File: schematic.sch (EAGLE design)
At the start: 56 parts, among them J1 FTDI_DEVICERA_SMT, M1 WIRELESS-NRF24L01, Q1 8MHz, T1 NMOS, T2 NMOS, T3 NMOS, T4 NMOS, U1 ATMEGA328P_TQFP, U2 GY-521MPU6050, U3 LTC3534

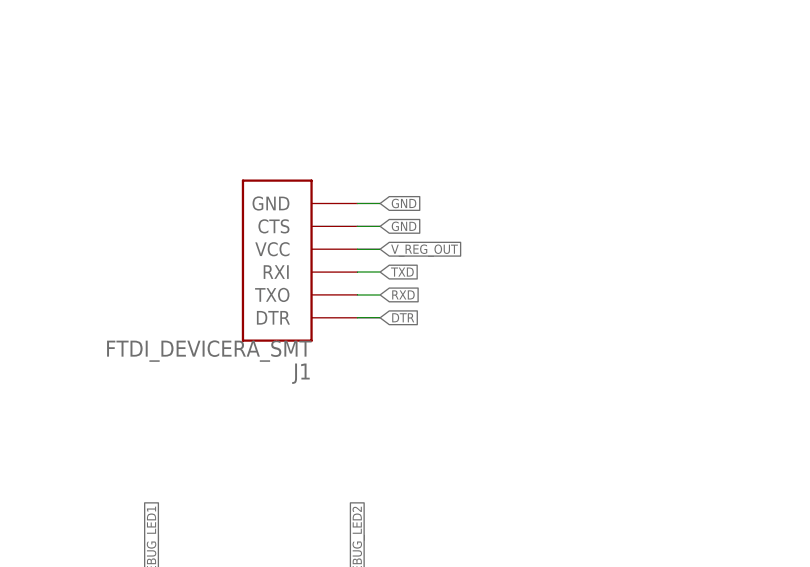
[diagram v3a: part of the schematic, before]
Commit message: fixed programmer RX TX
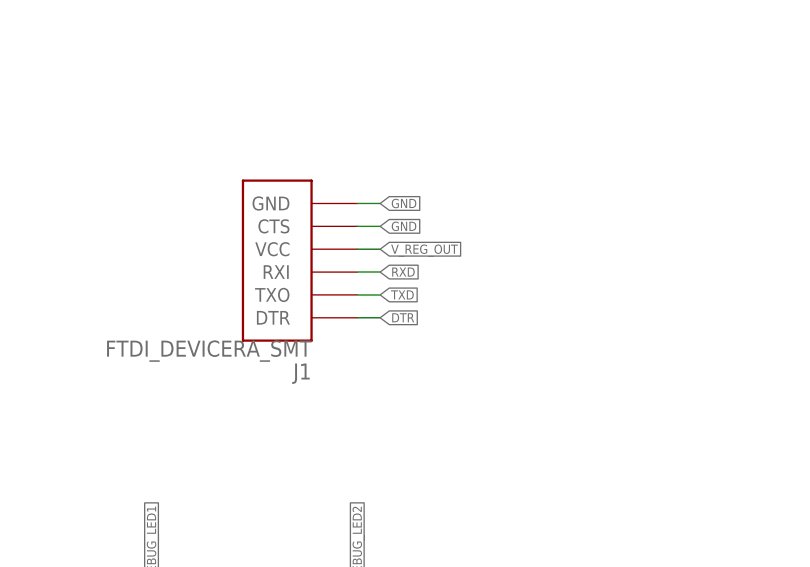
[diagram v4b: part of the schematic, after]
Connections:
- net RXD: now also J1.RXI; no longer J1.TXO
- net TXD: now also J1.TXO; no longer J1.RXI
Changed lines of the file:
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@@
 <net name="TXD" class="0">
-<segment>
-<pinref part="J1" gate="G$1" pin="RXI"/>
-<wire x1="-38.1" y1="15.24" x2="-35.56" y2="15.24" width="0.1524" layer="91"/>
-<label x="-35.56" y="15.24" size="1.016" layer="95" ratio="4" xref="yes"/>
-</segment>
 <segment>
 <pinref part="U1" gate="U$1" pin="PD1(TXD)"/>
@@
 <label x="228.6" y="81.28" size="1.016" layer="95" ratio="4" xref="yes"/>
 </segment>
-</net>
-<net name="RXD" class="0">
 <segment>
 <pinref part="J1" gate="G$1" pin="TXO"/>
 <wire x1="-38.1" y1="12.7" x2="-35.56" y2="12.7" width="0.1524" layer="91"/>
-<label x="-35.56" y="12.7" size="1.016" layer="95" ratio="4" xref="yes"/>
+<label x="-35.56" y="12.7" size="1.016" layer="95" xref="yes"/>
 </segment>
+</net>
+<net name="RXD" class="0">
 <segment>
 <pinref part="U1" gate="U$1" pin="PD0(RXD)"/>
@@
 <label x="228.6" y="83.82" size="1.016" layer="95" ratio="4" xref="yes"/>
 </segment>
+<segment>
+<pinref part="J1" gate="G$1" pin="RXI"/>
+<wire x1="-38.1" y1="15.24" x2="-35.56" y2="15.24" width="0.1524" layer="91"/>
+<label x="-35.56" y="15.24" size="1.016" layer="95" xref="yes"/>
+</segment>
 </net>

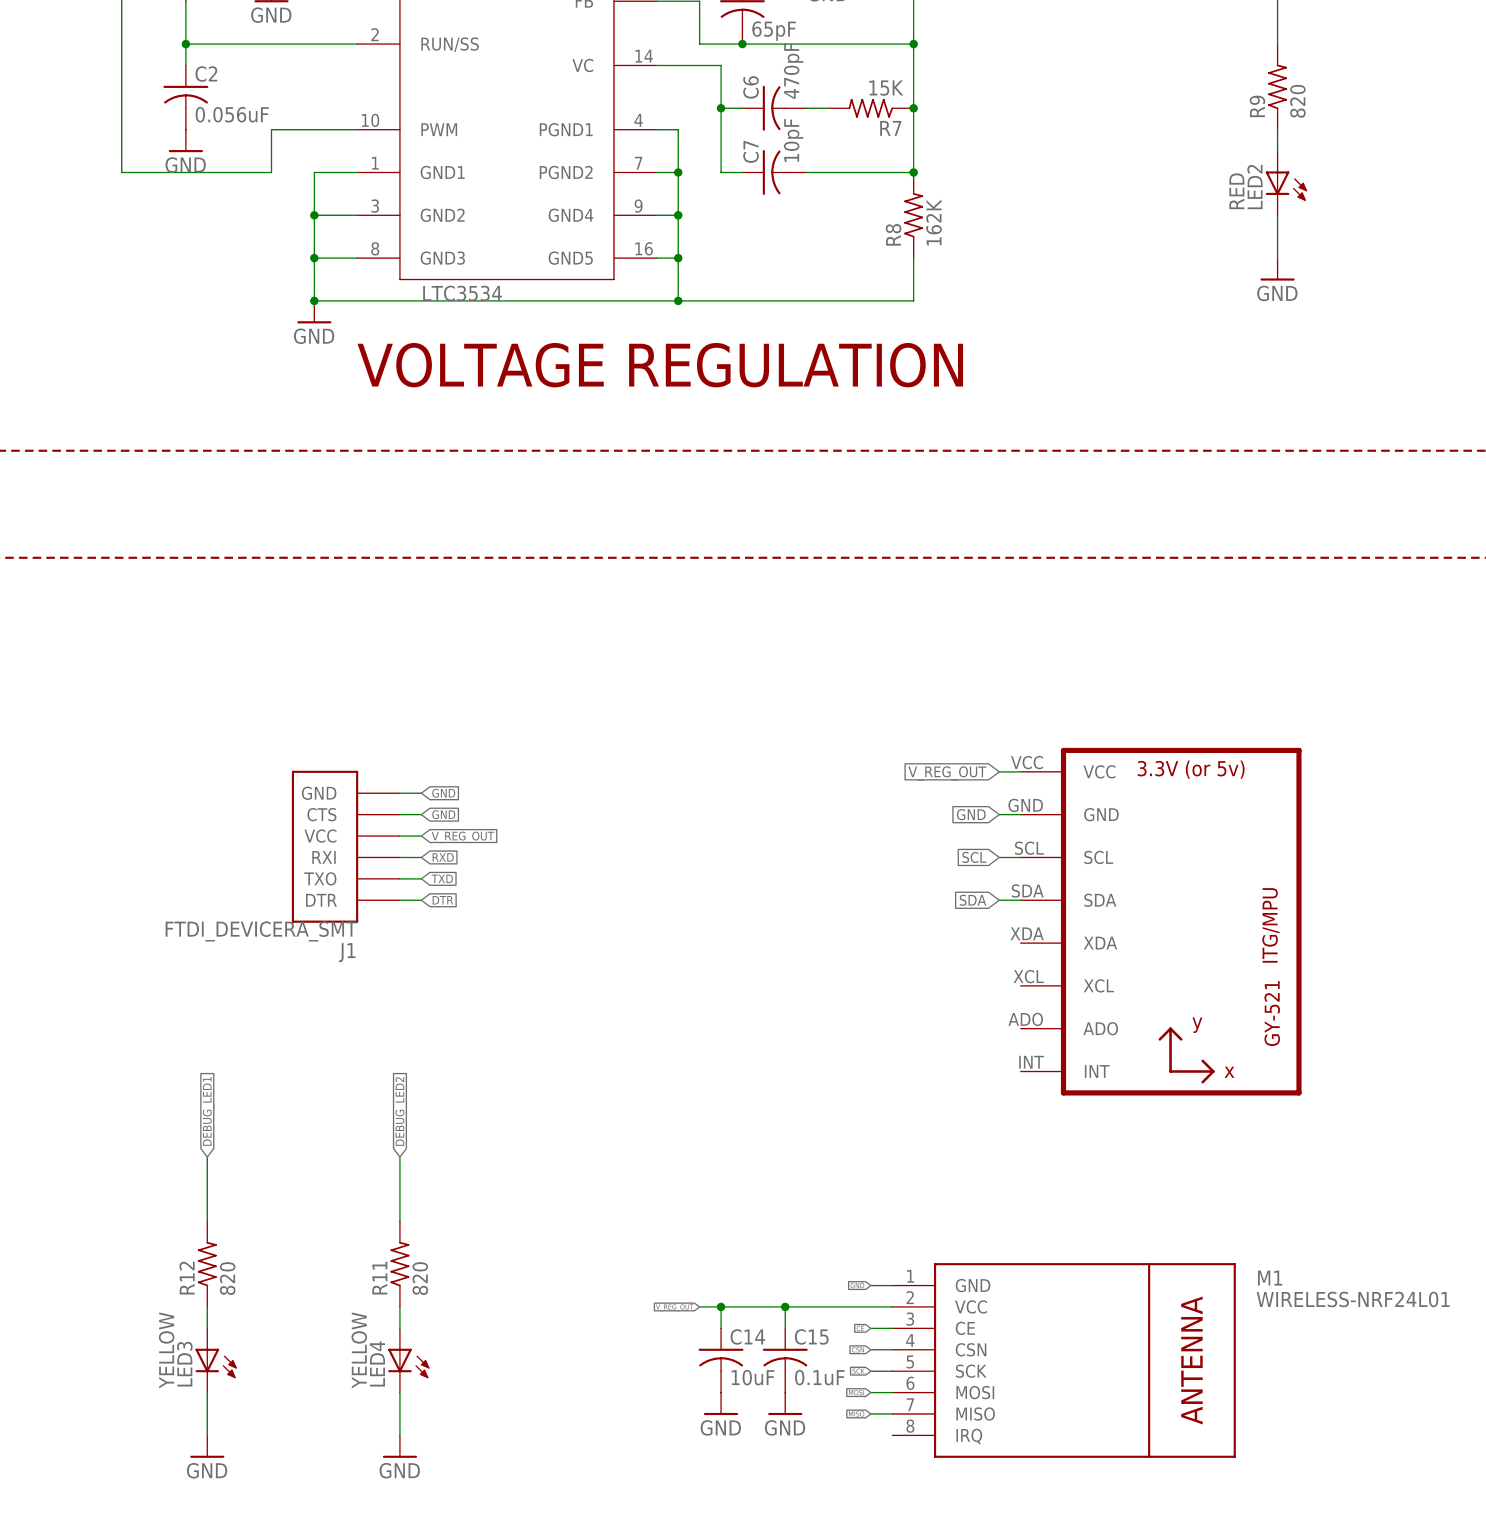
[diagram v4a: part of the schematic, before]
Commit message: Fixed LED package
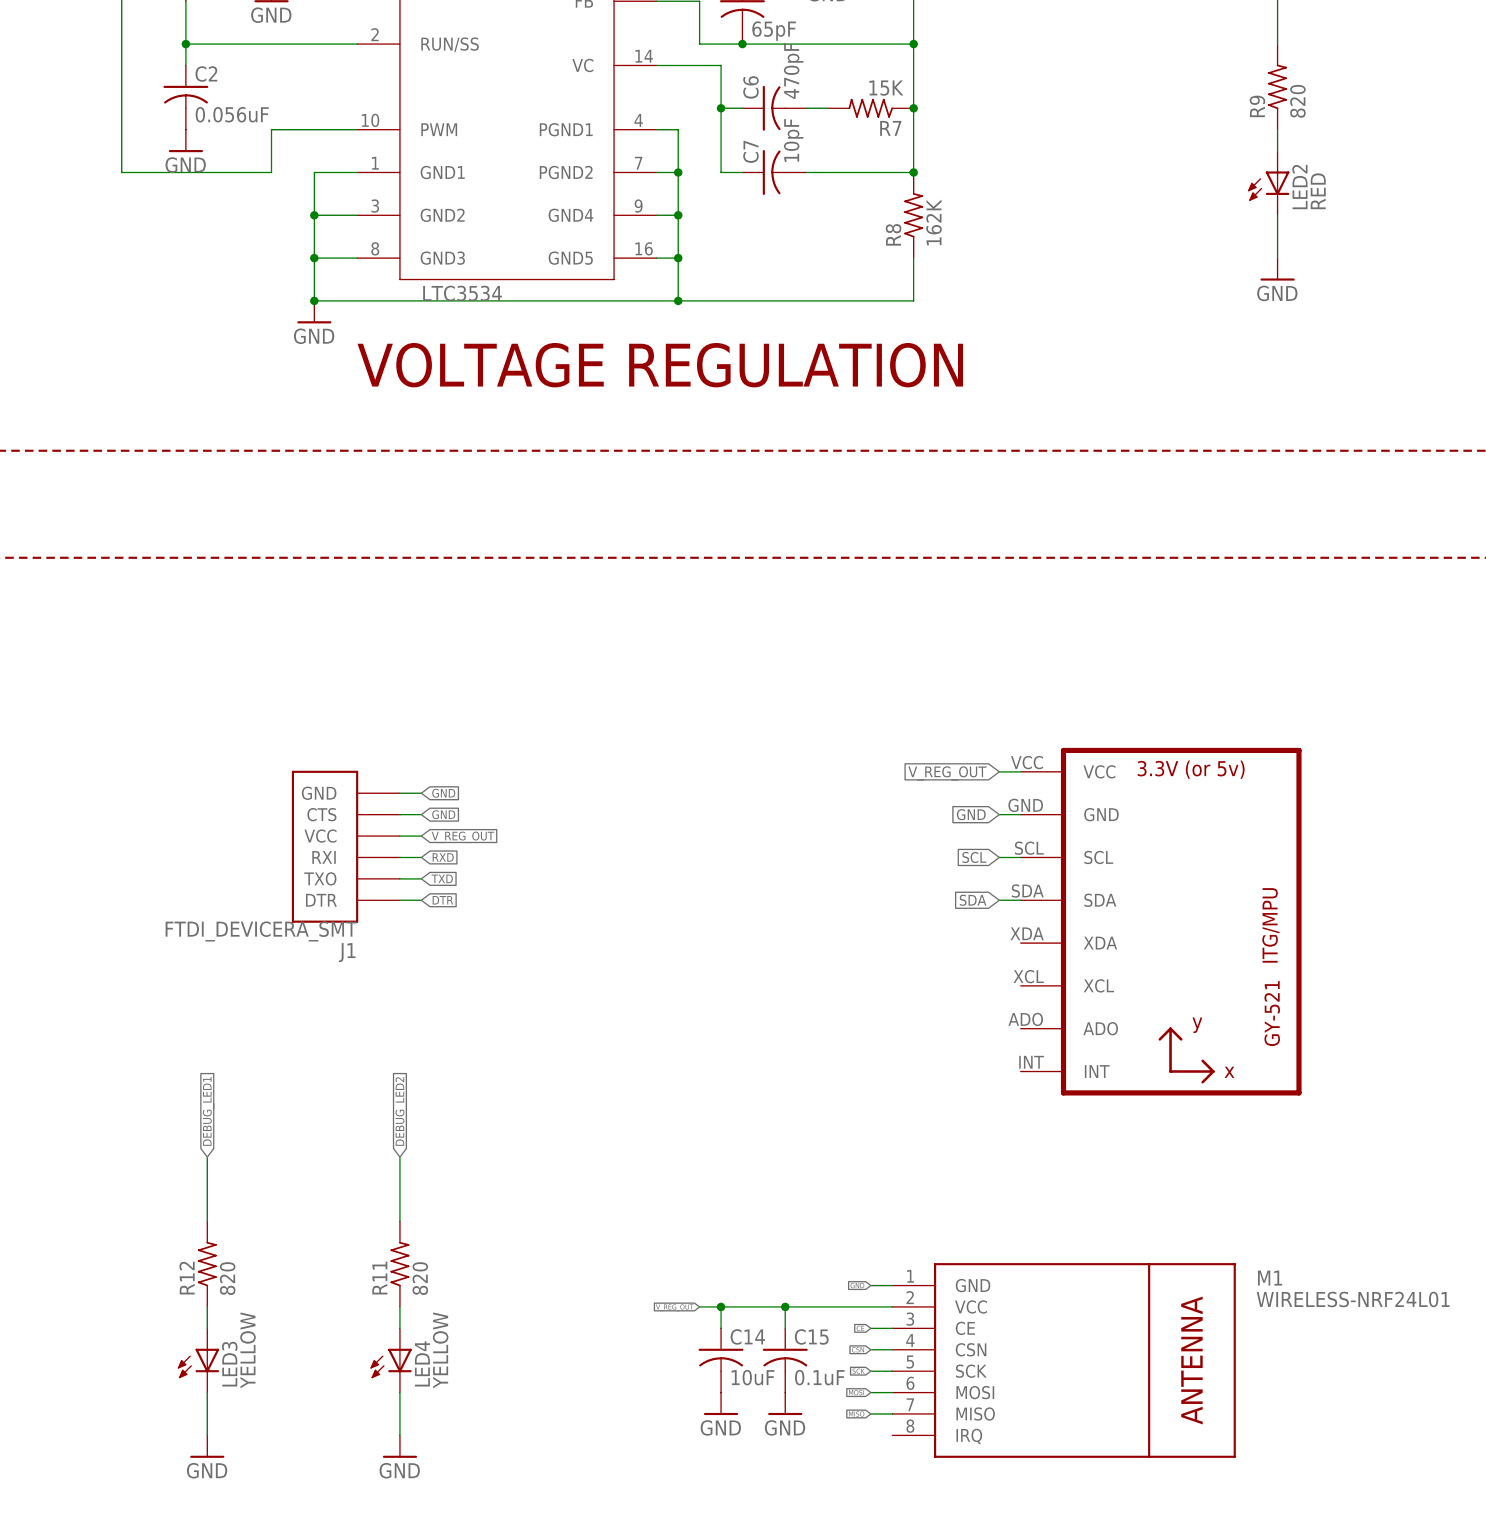
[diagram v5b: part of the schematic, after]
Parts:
- LED3, LED4: device led:LED -> led:LEDSML0603
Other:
- moved on the sheet: LED2, LED3, LED4
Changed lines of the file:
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@@
 <part name="GND28" library="SparkFun" deviceset="GND" device=""/>
 <part name="GND29" library="SparkFun" deviceset="GND" device=""/>
-<part name="LED3" library="led" library_urn="urn:adsk.eagle:library:259" deviceset="LED" device="" package3d_urn="urn:adsk.eagle:package:15825/1" value="YELLOW"/>
 <part name="GND30" library="SparkFun" deviceset="GND" device=""/>
-<part name="LED4" library="led" library_urn="urn:adsk.eagle:library:259" deviceset="LED" device="" package3d_urn="urn:adsk.eagle:package:15825/1" value="YELLOW"/>
 <part name="GND31" library="SparkFun" deviceset="GND" device=""/>
 <part name="GND32" library="SparkFun" deviceset="GND" device=""/>
@@
 <part name="R12" library="rcl" library_urn="urn:adsk.eagle:library:334" deviceset="R-US_" device="R0603" package3d_urn="urn:adsk.eagle:package:23555/2" value="820"/>
 <part name="R11" library="rcl" library_urn="urn:adsk.eagle:library:334" deviceset="R-US_" device="R0603" package3d_urn="urn:adsk.eagle:package:23555/2" value="820"/>
-<part name="LED1" library="led" library_urn="urn:adsk.eagle:library:259" deviceset="LED" device="SML0603" package3d_urn="urn:adsk.eagle:package:15832/1" value="RED"/>
-<part name="LED2" library="led" library_urn="urn:adsk.eagle:library:259" deviceset="LED" device="SML0603" package3d_urn="urn:adsk.eagle:package:15832/1" value="RED"/>
 <part name="R10" library="resistor" library_urn="urn:adsk.eagle:library:348" deviceset="R-US_" device="R0603" package3d_urn="urn:adsk.eagle:package:26057/1" value="10K"/>
 <part name="R13" library="resistor" library_urn="urn:adsk.eagle:library:348" deviceset="R-US_" device="R0603" package3d_urn="urn:adsk.eagle:package:26057/1" value="10K"/>
@@
 <part name="R16" library="resistor" library_urn="urn:adsk.eagle:library:348" deviceset="R-US_" device="R0603" package3d_urn="urn:adsk.eagle:package:26057/1" value="10K"/>
 <part name="C4" library="rcl" library_urn="urn:adsk.eagle:library:334" deviceset="C-US" device="C1206" package3d_urn="urn:adsk.eagle:package:23618/2" value="65pF"/>
+<part name="LED1" library="led" library_urn="urn:adsk.eagle:library:259" deviceset="LED" device="SML0603" package3d_urn="urn:adsk.eagle:package:15832/1" value="RED"/>
+<part name="LED2" library="led" library_urn="urn:adsk.eagle:library:259" deviceset="LED" device="SML0603" package3d_urn="urn:adsk.eagle:package:15832/1" value="RED"/>
+<part name="LED3" library="led" library_urn="urn:adsk.eagle:library:259" deviceset="LED" device="SML0603" package3d_urn="urn:adsk.eagle:package:15832/1" value="YELLOW"/>
+<part name="LED4" library="led" library_urn="urn:adsk.eagle:library:259" deviceset="LED" device="SML0603" package3d_urn="urn:adsk.eagle:package:15832/1" value="YELLOW"/>
 </parts>
 <sheets>
@@
 <instance part="GND28" gate="1" x="-193.04" y="-73.66"/>
 <instance part="GND29" gate="1" x="-144.78" y="-73.66"/>
-<instance part="LED3" gate="G$1" x="-60.96" y="-43.18" rot="MR0"/>
 <instance part="GND30" gate="1" x="-60.96" y="-55.88"/>
-<instance part="LED4" gate="G$1" x="-38.1" y="-43.18" rot="MR0"/>
 <instance part="GND31" gate="1" x="-38.1" y="-55.88"/>
 <instance part="GND32" gate="1" x="172.72" y="63.5"/>
@@
 <instance part="R12" gate="G$1" x="-60.96" y="-33.02" rot="R90"/>
 <instance part="R11" gate="G$1" x="-38.1" y="-33.02" rot="R90"/>
-<instance part="LED1" gate="G$1" x="-175.26" y="104.14" rot="MR270"/>
-<instance part="LED2" gate="G$1" x="66.04" y="96.52" rot="MR0"/>
 <instance part="R10" gate="G$1" x="139.7" y="111.76" rot="R90"/>
 <instance part="R13" gate="G$1" x="-193.04" y="-2.54" rot="R90"/>
@@
 <instance part="R16" gate="G$1" x="-144.78" y="-66.04" rot="R90"/>
 <instance part="C4" gate="G$1" x="2.54" y="116.84"/>
+<instance part="LED1" gate="G$1" x="-175.26" y="104.14" rot="MR270"/>
+<instance part="LED2" gate="G$1" x="66.04" y="96.52"/>
+<instance part="LED3" gate="G$1" x="-60.96" y="-43.18"/>
+<instance part="LED4" gate="G$1" x="-38.1" y="-43.18"/>
 </instances>
 <busses>
@@
 </segment>
 <segment>
-<pinref part="LED3" gate="G$1" pin="C"/>
 <pinref part="GND30" gate="1" pin="GND"/>
 <wire x1="-60.96" y1="-48.26" x2="-60.96" y2="-53.34" width="0.1524" layer="91"/>
-</segment>
-<segment>
-<pinref part="LED4" gate="G$1" pin="C"/>
+<pinref part="LED3" gate="G$1" pin="C"/>
+</segment>
+<segment>
 <pinref part="GND31" gate="1" pin="GND"/>
 <wire x1="-38.1" y1="-48.26" x2="-38.1" y2="-53.34" width="0.1524" layer="91"/>
+<pinref part="LED4" gate="G$1" pin="C"/>
 </segment>
 <segment>
@@
 <net name="N$12" class="0">
 <segment>
-<pinref part="LED3" gate="G$1" pin="A"/>
 <wire x1="-60.96" y1="-38.1" x2="-60.96" y2="-40.64" width="0.1524" layer="91"/>
 <pinref part="R12" gate="G$1" pin="1"/>
+<pinref part="LED3" gate="G$1" pin="A"/>
 </segment>
 </net>
 <net name="N$13" class="0">
 <segment>
-<pinref part="LED4" gate="G$1" pin="A"/>
 <wire x1="-38.1" y1="-38.1" x2="-38.1" y2="-40.64" width="0.1524" layer="91"/>
 <pinref part="R11" gate="G$1" pin="1"/>
-</segment>
-</net>
+<pinref part="LED4" gate="G$1" pin="A"/>
+</segment>
+</net>
